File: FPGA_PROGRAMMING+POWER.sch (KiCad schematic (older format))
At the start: 28 parts, among them U301 iCE40-HX4K-TQ144, U302 25LC_EEPROM

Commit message: Minor fixes and the gitignore was removed
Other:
- moved on the sheet: C314, C315, C316, C317
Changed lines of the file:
@@
 L C C316
 U 1 1 58DD57B1
-P 8750 1900
-F 0 "C316" H 8775 2000 50  0000 L CNN
-F 1 "100n" H 8775 1800 50  0000 L CNN
-F 2 "" H 8788 1750 50  0001 C CNN
-F 3 "" H 8750 1900 50  0001 C CNN
-	1    8750 1900
-	1    0    0    -1
-$EndComp
-$Comp
-L C C314
-U 1 1 58DD5824
-P 8150 2000
-F 0 "C314" H 8175 2100 50  0000 L CNN
-F 1 "100n" H 8175 1900 50  0000 L CNN
-F 2 "" H 8188 1850 50  0001 C CNN
-F 3 "" H 8150 2000 50  0001 C CNN
-	1    8150 2000
+P 8800 2000
+F 0 "C316" H 8825 2100 50  0000 L CNN
+F 1 "100n" H 8825 1900 50  0000 L CNN
+F 2 "" H 8838 1850 50  0001 C CNN
+F 3 "" H 8800 2000 50  0001 C CNN
+	1    8800 2000
 	1    0    0    -1
 $EndComp
@@
 L CP1 C315
 U 1 1 58DD5858
-P 8400 2000
-F 0 "C315" H 8425 2100 50  0000 L CNN
-F 1 "CP1" H 8425 1900 50  0000 L CNN
-F 2 "" H 8400 2000 50  0001 C CNN
-F 3 "" H 8400 2000 50  0001 C CNN
-	1    8400 2000
+P 8400 2100
+F 0 "C315" H 8425 2200 50  0000 L CNN
+F 1 "CP1" H 8425 2000 50  0000 L CNN
+F 2 "" H 8400 2100 50  0001 C CNN
+F 3 "" H 8400 2100 50  0001 C CNN
+	1    8400 2100
 	1    0    0    -1
 $EndComp
@@
 	1    9550 1500
 	0    1    1    0
-$EndComp
-$Comp
-L CP1 C317
-U 1 1 58DD5901
-P 9100 1900
-F 0 "C317" H 9125 2000 50  0000 L CNN
-F 1 "CP1" H 9125 1800 50  0000 L CNN
-F 2 "" H 9100 1900 50  0001 C CNN
-F 3 "" H 9100 1900 50  0001 C CNN
-	1    9100 1900
-	1    0    0    -1
 $EndComp
 $Comp
@@
 Connection ~ 9750 1500
 Wire Wire Line
-	7550 1750 9400 1750
-Connection ~ 9100 1750
-Connection ~ 8750 1750
-Wire Wire Line
-	8400 1850 8400 1500
+	8400 1500 8400 1950
 Wire Wire Line
 	8400 1500 9400 1500
 Wire Wire Line
-	7550 1850 8400 1850
-Connection ~ 8150 1850
-Wire Wire Line
-	8150 2150 8400 2150
-Wire Wire Line
-	8750 2050 9100 2050
-Wire Wire Line
-	8300 2150 8300 3150
-Wire Wire Line
 	8300 3150 7550 3150
-Connection ~ 8300 2150
-Wire Wire Line
-	8950 2050 8950 3050
 Wire Wire Line
 	8950 3050 7550 3050
-Connection ~ 8950 2050
 Wire Wire Line
 	7550 2250 7850 2250
@@
 Text Notes 2600 4250 0    60   ~ 12
 DECOUPLING
+$Comp
+L C C314
+U 1 1 58DD5824
+P 8150 2100
+F 0 "C314" H 8175 2200 50  0000 L CNN
+F 1 "100n" H 8175 2000 50  0000 L CNN
+F 2 "" H 8188 1950 50  0001 C CNN
+F 3 "" H 8150 2100 50  0001 C CNN
+	1    8150 2100
+	1    0    0    -1
+$EndComp
+Wire Wire Line
+	8150 1950 8150 1850
+Wire Wire Line
+	7550 1850 8400 1850
+Connection ~ 8400 1850
+Connection ~ 8150 1850
+Wire Wire Line
+	8150 2250 8150 2400
+Wire Wire Line
+	8150 2400 8400 2400
+Wire Wire Line
+	8400 2400 8400 2250
+Wire Wire Line
+	8300 3150 8300 2400
+Connection ~ 8300 2400
+$Comp
+L CP1 C317
+U 1 1 58DD5901
+P 9100 2000
+F 0 "C317" H 9125 2100 50  0000 L CNN
+F 1 "CP1" H 9125 1900 50  0000 L CNN
+F 2 "" H 9100 2000 50  0001 C CNN
+F 3 "" H 9100 2000 50  0001 C CNN
+	1    9100 2000
+	1    0    0    -1
+$EndComp
+Wire Wire Line
+	7550 1750 9400 1750
+Wire Wire Line
+	9100 1850 9100 1750
+Connection ~ 9100 1750
+Wire Wire Line
+	8800 1850 8800 1750
+Connection ~ 8800 1750
+Wire Wire Line
+	8800 2150 8800 2300
+Wire Wire Line
+	8800 2300 9100 2300
+Wire Wire Line
+	9100 2300 9100 2150
+Wire Wire Line
+	8950 3050 8950 2300
+Connection ~ 8950 2300
 $EndSCHEMATC

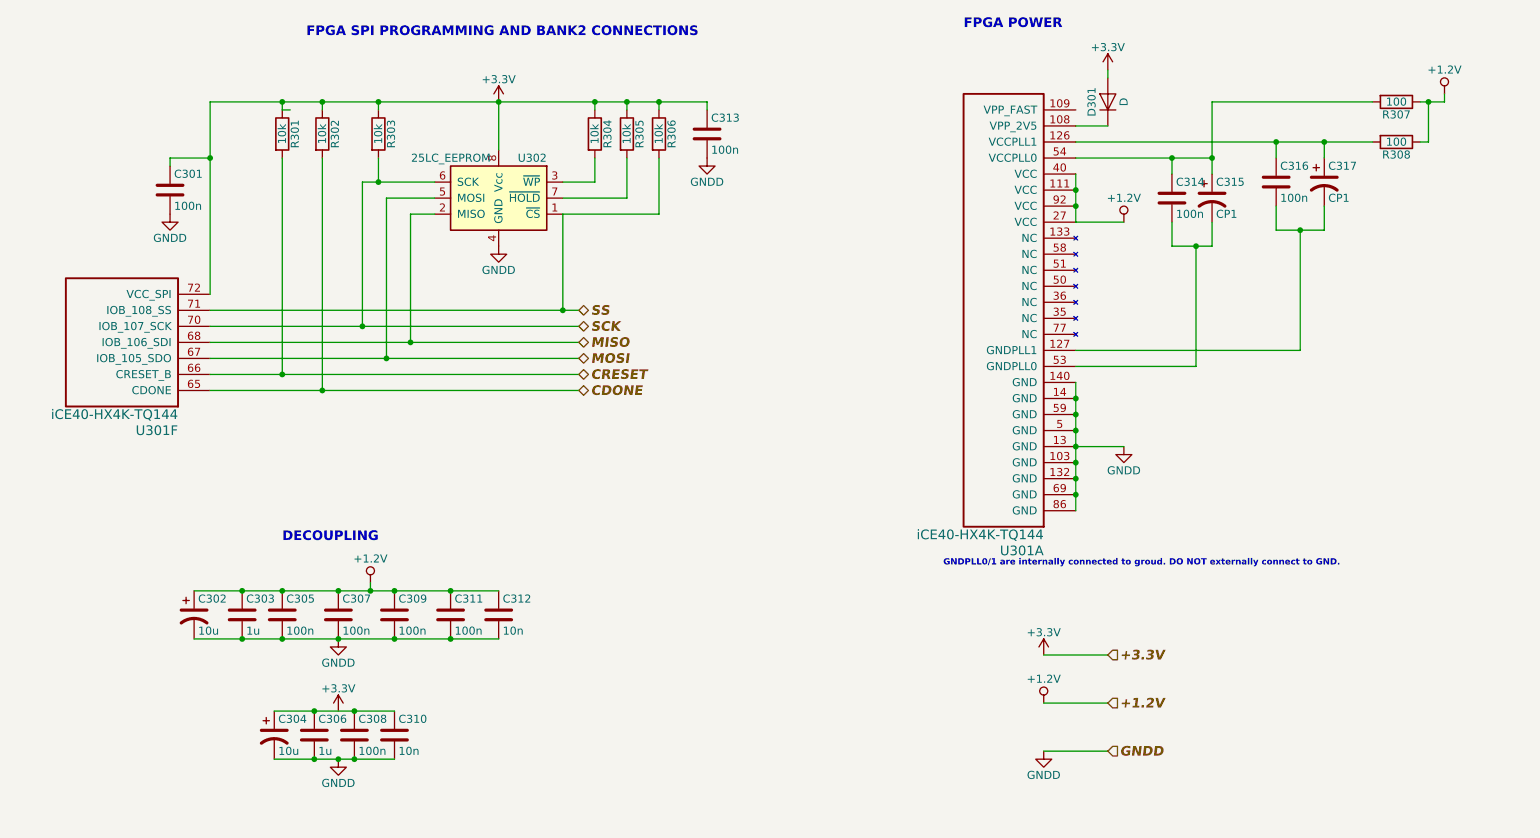
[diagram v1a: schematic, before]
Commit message: Added part number and specifications on all sheets
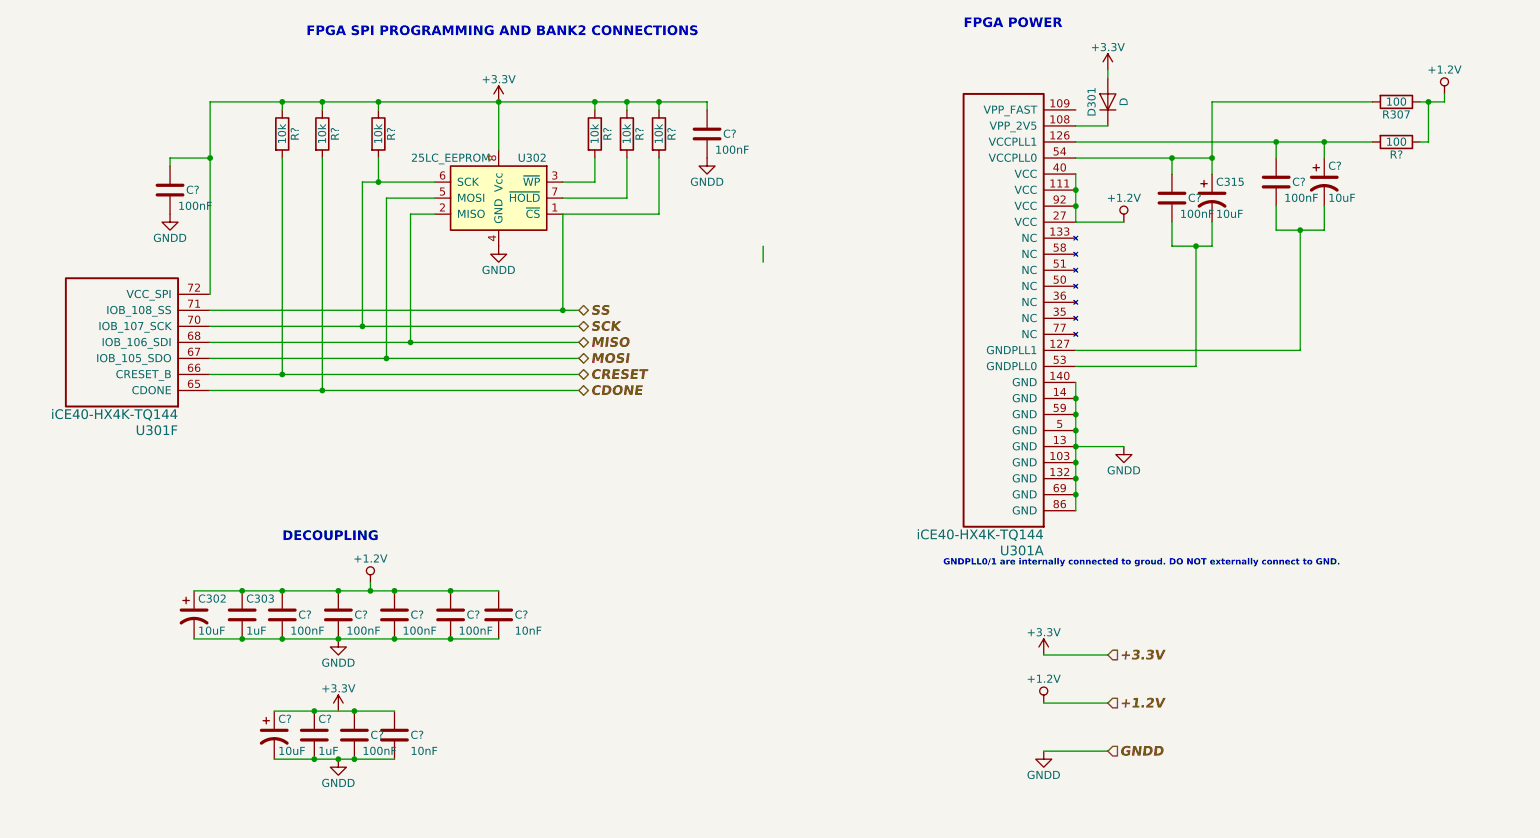
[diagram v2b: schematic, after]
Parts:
- removed C301, C305, C307, C308, C309, C311, C313, C314, C316: 100n, symbol C
- removed C304: 10u, symbol CP1
- removed C306: 1u, symbol C
- removed C310, C312: 10n, symbol C
- removed C317: CP1, symbol CP1
- removed R301, R302, R303, R304, R305, R306: 10k, symbol R
- removed R308: 100, symbol R
- added C? (x9): 100nF, Capacitors_SMD:C_0603_HandSoldering, symbol C
- added C? (x2): 10nF, Capacitors_SMD:C_0603_HandSoldering, symbol C
- added C?: 1uF, Capacitors_SMD:C_0603_HandSoldering, symbol C
- added C? (x2): 10uF, Capacitors_SMD:C_1206_HandSoldering, symbol CP1
- added R? (x6): 10k, Resistors_SMD:R_0603_HandSoldering, symbol R
- added R?: 100, Resistors_SMD:R_0603_HandSoldering, symbol R
- C302: value 10u -> 10uF; footprint (none) -> Capacitors_SMD:C_1206_HandSoldering; Manufacturer Part (none) -> TAJA106K010RNJV
- C303: value 1u -> 1uF; footprint (none) -> Capacitors_SMD:C_0603_HandSoldering; Ceramic (none) -> X5R; Manufacturer Part (none) -> C0603C105K8PACTU; VDC (none) -> 10V
- C315: value CP1 -> 10uF; footprint (none) -> Capacitors_SMD:C_1206_HandSoldering; Manufacturer Part (none) -> TAJA106K010RNJV; VDC (none) -> 10V
- D301: footprint (none) -> Diodes_SMD:D_SOT-23_ANK; Manufacturer Part (none) -> BAS21,215
- R307: footprint (none) -> Resistors_SMD:R_0603_HandSoldering; Manufacturer Part (none) -> CRCW0603100RFKEA
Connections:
- net +1.2V: now also C?.1, C?.1, C?.1, C?.1, C?.1, R?.1
- net +3V3: now also C?.1, C?.1, R?.1, R?.1, R?.1, R?.1, R?.1, R?.1
- net CDONE: now also R?.2
- net CRESET: now also R?.2
- net GNDD: now also C?.2, C?.2, C?.2, C?.2, C?.2, C?.2, C?.2, C?.2, C?.2, C?.2, C?.2
- net SCK: now also R?.2
- net SS: now also R?.2
- net at U302.3 (~WP): now also R?.2
- net at U302.7 (~HOLD): now also R?.2
- net at U301.126 (VCCPLL1): now also C?.1, C?.1, R?.2
- net at U301.127 (GNDPLL1): now also C?.2, C?.2
- net at C315.1, R307.2, U301.54 (VCCPLL0): now also C?.1
- net at C315.2, U301.53 (GNDPLL0): now also C?.2
- new net: C?.1, C?.1, C?.1, C?.1

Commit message: Reordered connections again. Option 1: RAM at left bank, some connections at left and top banks.
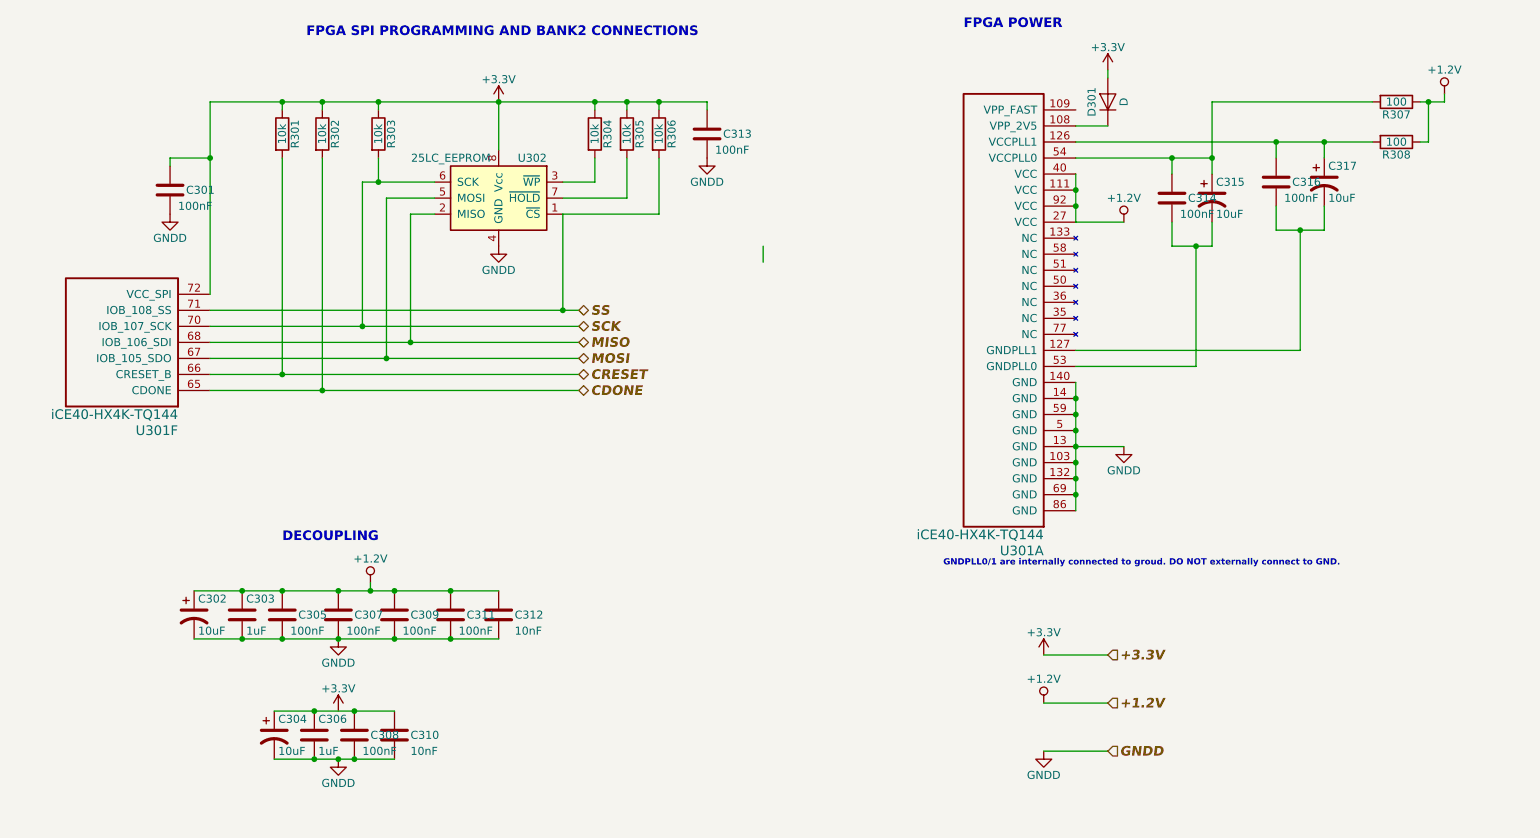
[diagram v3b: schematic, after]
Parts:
- gave numbers to parts that had none: 21
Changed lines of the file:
@@
 	5600 2400 5600 2500
 $Comp
-L C C?
+L C C313
 U 1 1 58E870BB
 P 5250 1700
-F 0 "C?" H 5350 1700 50  0000 L CNN
+F 0 "C313" H 5350 1700 50  0000 L CNN
 F 1 "100nF" H 5300 1600 50  0000 L CNN
 F 2 "Capacitors_SMD:C_0603_HandSoldering" H 5288 1550 50  0001 C CNN
@@
 $EndComp
 $Comp
-L R R?
+L R R301
 U 1 1 58E87314
 P 2600 1700
-F 0 "R?" V 2680 1700 50  0000 C CNN
+F 0 "R301" V 2680 1700 50  0000 C CNN
 F 1 "10k" V 2600 1700 50  0000 C CNN
 F 2 "Resistors_SMD:R_0603_HandSoldering" V 2530 1700 50  0001 C CNN
@@
 $EndComp
 $Comp
-L R R?
+L R R302
 U 1 1 58E87513
 P 2850 1700
-F 0 "R?" V 2930 1700 50  0000 C CNN
+F 0 "R302" V 2930 1700 50  0000 C CNN
 F 1 "10k" V 2850 1700 50  0000 C CNN
 F 2 "Resistors_SMD:R_0603_HandSoldering" V 2780 1700 50  0001 C CNN
@@
 $EndComp
 $Comp
-L R R?
+L R R303
 U 1 1 58E875DD
 P 3200 1700
-F 0 "R?" V 3280 1700 50  0000 C CNN
+F 0 "R303" V 3280 1700 50  0000 C CNN
 F 1 "10k" V 3200 1700 50  0000 C CNN
 F 2 "Resistors_SMD:R_0603_HandSoldering" V 3130 1700 50  0001 C CNN
@@
 $EndComp
 $Comp
-L R R?
+L R R304
 U 1 1 58E87667
 P 4550 1700
-F 0 "R?" V 4630 1700 50  0000 C CNN
+F 0 "R304" V 4630 1700 50  0000 C CNN
 F 1 "10k" V 4550 1700 50  0000 C CNN
 F 2 "Resistors_SMD:R_0603_HandSoldering" V 4480 1700 50  0001 C CNN
@@
 $EndComp
 $Comp
-L R R?
+L R R305
 U 1 1 58E8773D
 P 4750 1700
-F 0 "R?" V 4830 1700 50  0000 C CNN
+F 0 "R305" V 4830 1700 50  0000 C CNN
 F 1 "10k" V 4750 1700 50  0000 C CNN
 F 2 "Resistors_SMD:R_0603_HandSoldering" V 4680 1700 50  0001 C CNN
@@
 $EndComp
 $Comp
-L R R?
+L R R306
 U 1 1 58E87855
 P 4950 1700
-F 0 "R?" V 5030 1700 50  0000 C CNN
+F 0 "R306" V 5030 1700 50  0000 C CNN
 F 1 "10k" V 4950 1700 50  0000 C CNN
 F 2 "Resistors_SMD:R_0603_HandSoldering" V 4880 1700 50  0001 C CNN
@@
 $EndComp
 $Comp
-L C C?
+L C C305
 U 1 1 58E87CDC
 P 2600 4700
-F 0 "C?" H 2700 4700 50  0000 L CNN
+F 0 "C305" H 2700 4700 50  0000 L CNN
 F 1 "100nF" H 2650 4600 50  0000 L CNN
 F 2 "Capacitors_SMD:C_0603_HandSoldering" H 2638 4550 50  0001 C CNN
@@
 $EndComp
 $Comp
-L C C?
+L C C307
 U 1 1 58E87D86
 P 2950 4700
-F 0 "C?" H 3050 4700 50  0000 L CNN
+F 0 "C307" H 3050 4700 50  0000 L CNN
 F 1 "100nF" H 3000 4600 50  0000 L CNN
 F 2 "Capacitors_SMD:C_0603_HandSoldering" H 2988 4550 50  0001 C CNN
@@
 $EndComp
 $Comp
-L C C?
+L C C309
 U 1 1 58E87DFF
 P 3300 4700
-F 0 "C?" H 3400 4700 50  0000 L CNN
+F 0 "C309" H 3400 4700 50  0000 L CNN
 F 1 "100nF" H 3350 4600 50  0000 L CNN
 F 2 "Capacitors_SMD:C_0603_HandSoldering" H 3338 4550 50  0001 C CNN
@@
 $EndComp
 $Comp
-L C C?
+L C C311
 U 1 1 58E87E73
 P 3650 4700
-F 0 "C?" H 3750 4700 50  0000 L CNN
+F 0 "C311" H 3750 4700 50  0000 L CNN
 F 1 "100nF" H 3700 4600 50  0000 L CNN
 F 2 "Capacitors_SMD:C_0603_HandSoldering" H 3688 4550 50  0001 C CNN
@@
 $EndComp
 $Comp
-L C C?
+L C C308
 U 1 1 58E87F08
 P 3050 5450
-F 0 "C?" H 3150 5450 50  0000 L CNN
+F 0 "C308" H 3150 5450 50  0000 L CNN
 F 1 "100nF" H 3100 5350 50  0000 L CNN
 F 2 "Capacitors_SMD:C_0603_HandSoldering" H 3088 5300 50  0001 C CNN
@@
 $EndComp
 $Comp
-L C C?
+L C C314
 U 1 1 58E87FD8
 P 8150 2100
-F 0 "C?" H 8250 2100 50  0000 L CNN
+F 0 "C314" H 8250 2100 50  0000 L CNN
 F 1 "100nF" H 8200 2000 50  0000 L CNN
 F 2 "Capacitors_SMD:C_0603_HandSoldering" H 8188 1950 50  0001 C CNN
@@
 $EndComp
 $Comp
-L C C?
+L C C316
 U 1 1 58E8808E
 P 8800 2000
-F 0 "C?" H 8900 2000 50  0000 L CNN
+F 0 "C316" H 8900 2000 50  0000 L CNN
 F 1 "100nF" H 8850 1900 50  0000 L CNN
 F 2 "Capacitors_SMD:C_0603_HandSoldering" H 8838 1850 50  0001 C CNN
@@
 $EndComp
 $Comp
-L C C?
+L C C301
 U 1 1 58E8849D
 P 1900 2050
-F 0 "C?" H 2000 2050 50  0000 L CNN
+F 0 "C301" H 2000 2050 50  0000 L CNN
 F 1 "100nF" H 1950 1950 50  0000 L CNN
 F 2 "Capacitors_SMD:C_0603_HandSoldering" H 1938 1900 50  0001 C CNN
@@
 $EndComp
 $Comp
-L C C?
+L C C312
 U 1 1 58E88FCF
 P 3950 4700
-F 0 "C?" H 4050 4700 50  0000 L CNN
+F 0 "C312" H 4050 4700 50  0000 L CNN
 F 1 "10nF" H 4050 4600 50  0000 L CNN
 F 2 "Capacitors_SMD:C_0603_HandSoldering" H 3988 4550 50  0001 C CNN
@@
 $EndComp
 $Comp
-L C C?
+L C C310
 U 1 1 58E890DE
 P 3300 5450
-F 0 "C?" H 3400 5450 50  0000 L CNN
+F 0 "C310" H 3400 5450 50  0000 L CNN
 F 1 "10nF" H 3400 5350 50  0000 L CNN
 F 2 "Capacitors_SMD:C_0603_HandSoldering" H 3338 5300 50  0001 C CNN
@@
 $EndComp
 $Comp
-L C C?
+L C C306
 U 1 1 58E89314
 P 2800 5450
-F 0 "C?" H 2825 5550 50  0000 L CNN
+F 0 "C306" H 2825 5550 50  0000 L CNN
 F 1 "1uF" H 2825 5350 50  0000 L CNN
 F 2 "Capacitors_SMD:C_0603_HandSoldering" H 2838 5300 50  0001 C CNN
@@
 $EndComp
 $Comp
-L CP1 C?
+L CP1 C304
 U 1 1 58E89752
 P 2550 5450
-F 0 "C?" H 2575 5550 50  0000 L CNN
+F 0 "C304" H 2575 5550 50  0000 L CNN
 F 1 "10uF" H 2575 5350 50  0000 L CNN
 F 2 "Capacitors_SMD:C_1206_HandSoldering" H 2550 5450 50  0001 C CNN
@@
 $EndComp
 $Comp
-L CP1 C?
+L CP1 C317
 U 1 1 58E8A94C
 P 9100 2000
-F 0 "C?" H 9125 2100 50  0000 L CNN
+F 0 "C317" H 9125 2100 50  0000 L CNN
 F 1 "10uF" H 9125 1900 50  0000 L CNN
 F 2 "Capacitors_SMD:C_1206_HandSoldering" H 9100 2000 50  0001 C CNN
@@
 $EndComp
 $Comp
-L R R?
+L R R308
 U 1 1 58E8DB76
 P 9550 1750
-F 0 "R?" V 9630 1750 50  0000 C CNN
+F 0 "R308" V 9630 1750 50  0000 C CNN
 F 1 "100" V 9550 1750 50  0000 C CNN
 F 2 "Resistors_SMD:R_0603_HandSoldering" V 9480 1750 50  0001 C CNN

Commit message: Minnor fixes
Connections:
- net +3V3 is gone; now on net +3.3V: C301.1, C313.1, D301.2 (A), R301.1, R302.1, R303.1, R304.1, R305.1, R306.1, U301.72 (VCC_SPI), U302.8 (Vcc)
- net +3.3V: now reaches C304.1, C306.1, C308.1, C310.1
- no-connect marks 0 -> 8
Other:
- moved on the sheet: C302, C303, C304, C305, C306, C307, C308, C309, C310, C311, C312
